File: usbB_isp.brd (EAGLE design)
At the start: 100 x 80 mm, 12 parts, among them IC1 788TV, IC2 TINY13-20PU, X1 PN61729-S

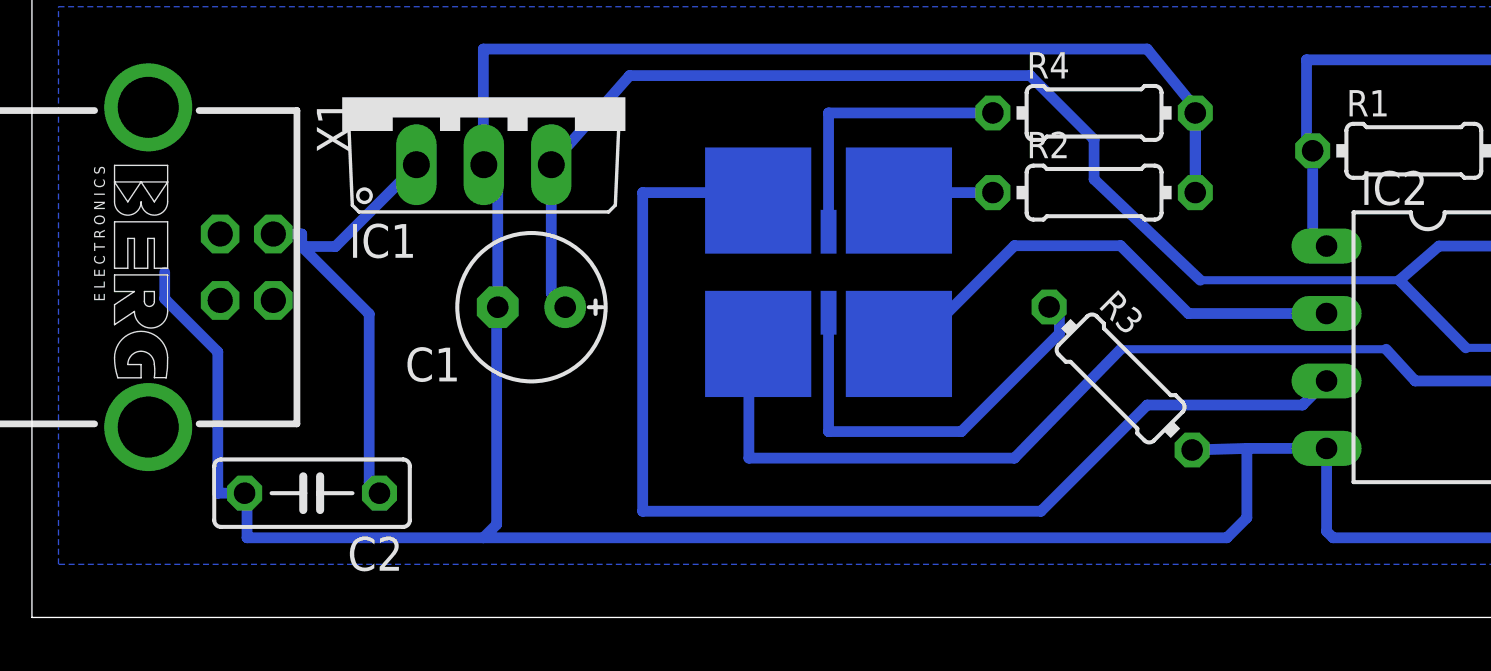
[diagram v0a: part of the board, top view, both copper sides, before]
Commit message: fixing usb-pins
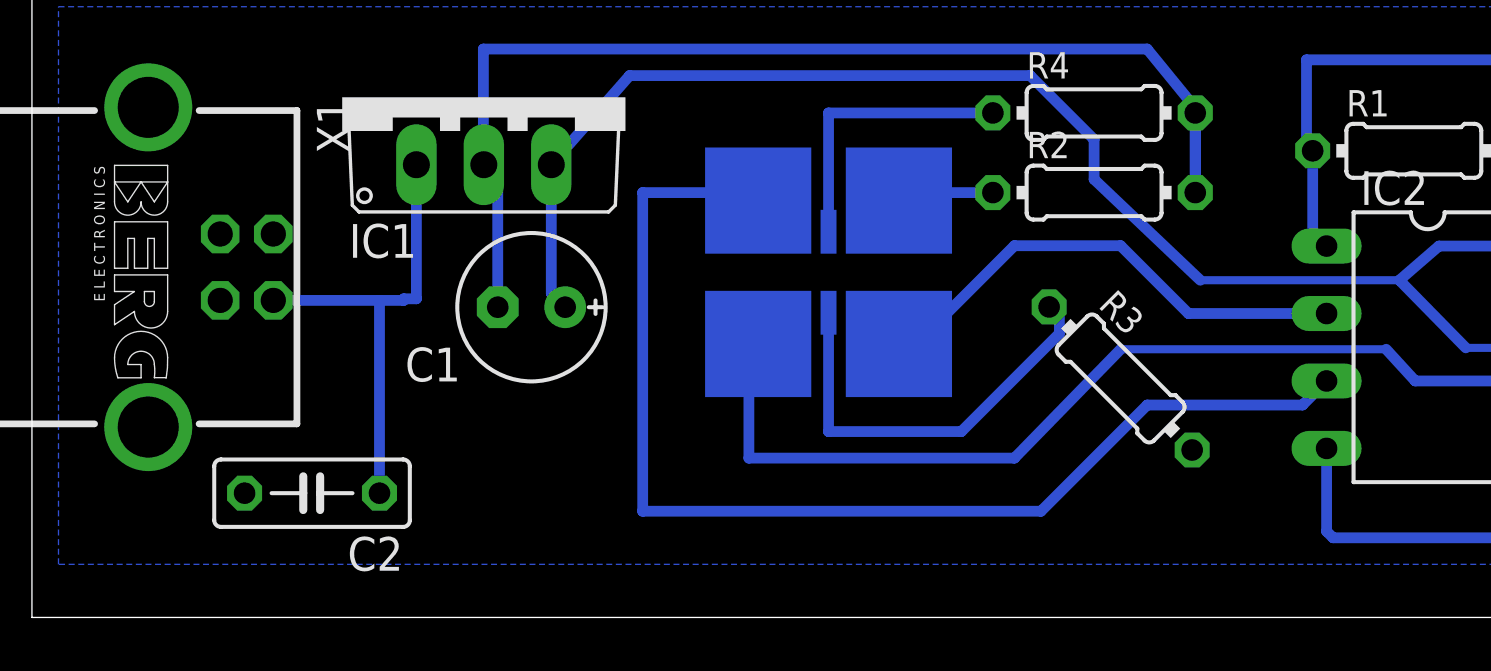
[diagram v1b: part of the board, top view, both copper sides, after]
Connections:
- net GND: now also X1.3; no longer X1.4
- net N$1: now also X1.1; no longer X1.2
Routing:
- net GND: track 160.9 -> 93.5 mm

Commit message: done stuff
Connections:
- net GND: no longer X1.3
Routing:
- net GND: track 93.5 -> 113.0 mm
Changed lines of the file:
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@@
 <wire x1="43.81" y1="19.19" x2="42" y2="21.4064" width="0.4064" layer="16"/>
 <wire x1="42" y1="21.4064" x2="17" y2="21.4064" width="0.4064" layer="16"/>
-<wire x1="17" y1="21.4064" x2="17" y2="17.068" width="0.4064" layer="16"/>
+<wire x1="17" y1="21.4064" x2="17" y2="21" width="0.4064" layer="16"/>
+<wire x1="17" y1="21" x2="17" y2="17.068" width="0.4064" layer="16"/>
 <wire x1="17" y1="17.068" x2="17.018" y2="17.05" width="0.4064" layer="16"/>
 <polygon width="0.4064" layer="16" isolate="0.5842" thermals="no">
@@
 </polygon>
 <contactref element="X1" pad="S1"/>
-<contactref element="X1" pad="3"/>
+<wire x1="4.38" y1="19.21" x2="4" y2="19.21" width="0.4064" layer="16"/>
+<wire x1="4" y1="19.21" x2="4" y2="21" width="0.4064" layer="16"/>
+<wire x1="4" y1="21" x2="17" y2="21" width="0.4064" layer="16"/>
+<wire x1="8.008" y1="4.68" x2="4" y2="4.68" width="0.4064" layer="16"/>
+<wire x1="4" y1="4.68" x2="4" y2="5" width="0.4064" layer="16"/>
 </signal>
 <signal name="VCC">
@@
 </signal>
 </signals>
-<errors>
-</errors>
 </board>
 </drawing>
